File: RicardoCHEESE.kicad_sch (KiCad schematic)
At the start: 37 parts, among them J101 RBUS, U101 ESP32-S3, Y101 40MHz±10ppm

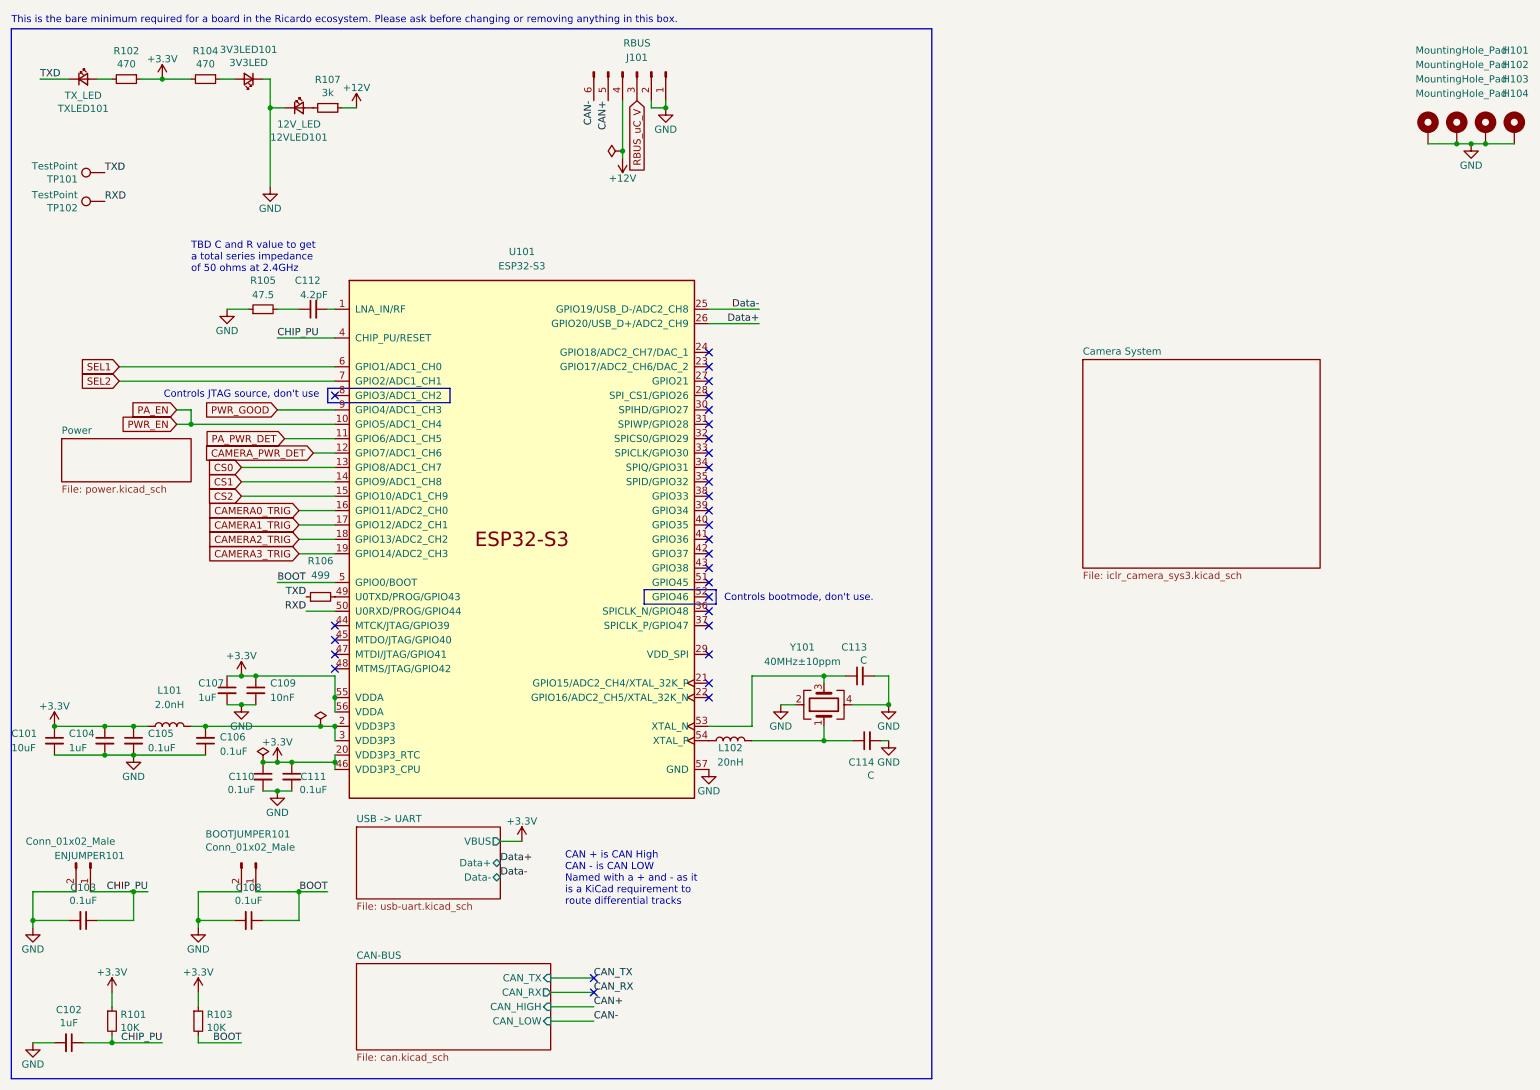
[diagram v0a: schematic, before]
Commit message: File names and ERC
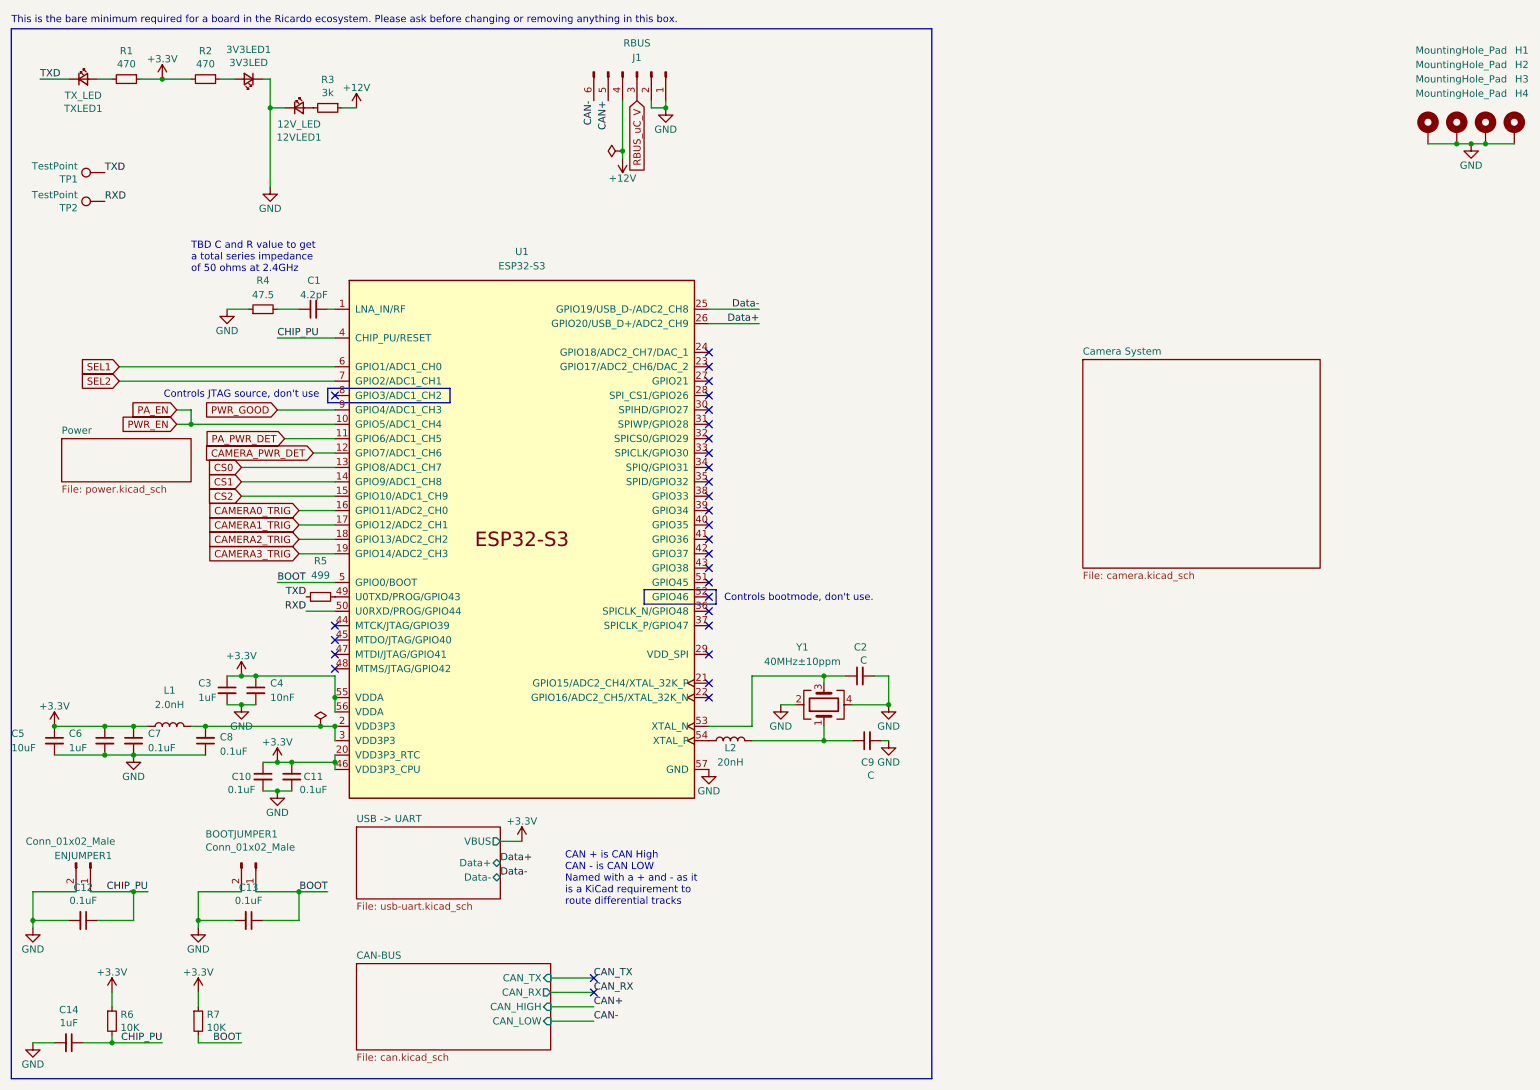
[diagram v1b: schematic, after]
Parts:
- renumbered 12VLED101 to 12VLED1, 3V3LED101 to 3V3LED1, BOOTJUMPER101 to BOOTJUMPER1, C112 to C1, C110 to C10, C111 to C11, C103 to C12, C108 to C13, C102 to C14, C113 to C2, C107 to C3, C109 to C4, C101 to C5, C104 to C6, C105 to C7, C106 to C8, C114 to C9, ENJUMPER101 to ENJUMPER1, H101 to H1, H102 to H2, H103 to H3, H104 to H4, J101 to J1, L101 to L1, L102 to L2, R102 to R1, R104 to R2, R107 to R3, R105 to R4, R106 to R5, R101 to R6, R103 to R7, TP101 to TP1, TP102 to TP2, TXLED101 to TXLED1, U101 to U1, Y101 to Y1
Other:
- sheet Camera System: file iclr_camera_sys3.kicad_sch -> camera.kicad_sch

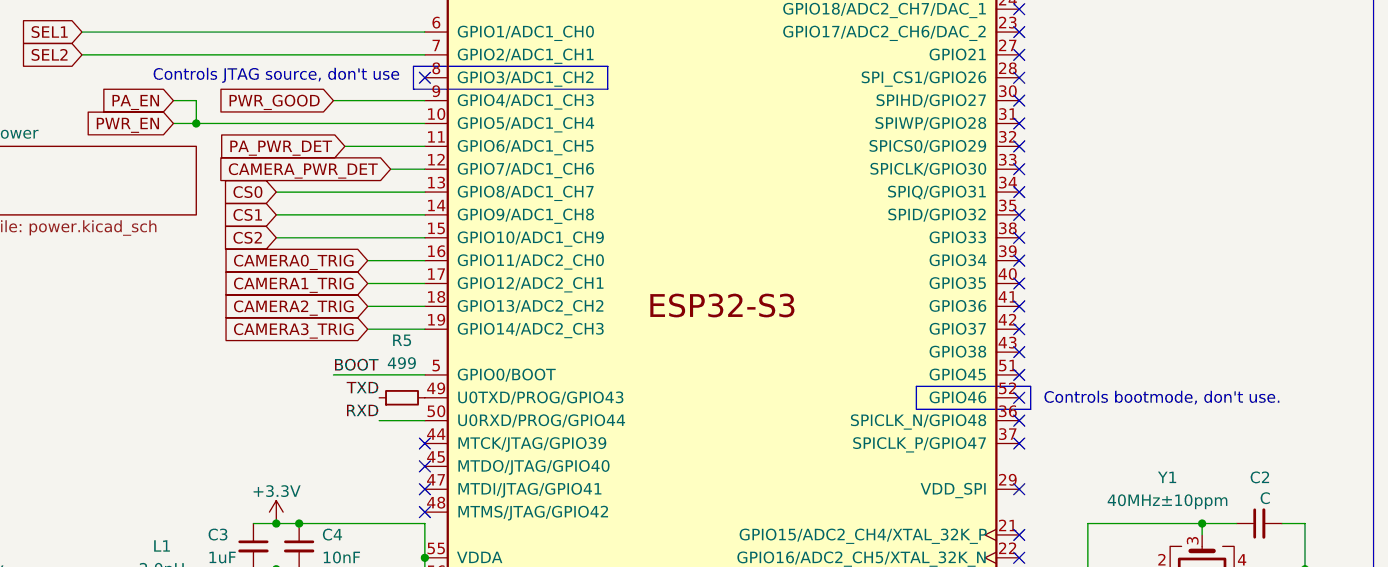
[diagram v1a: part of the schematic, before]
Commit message: Add photo triggers
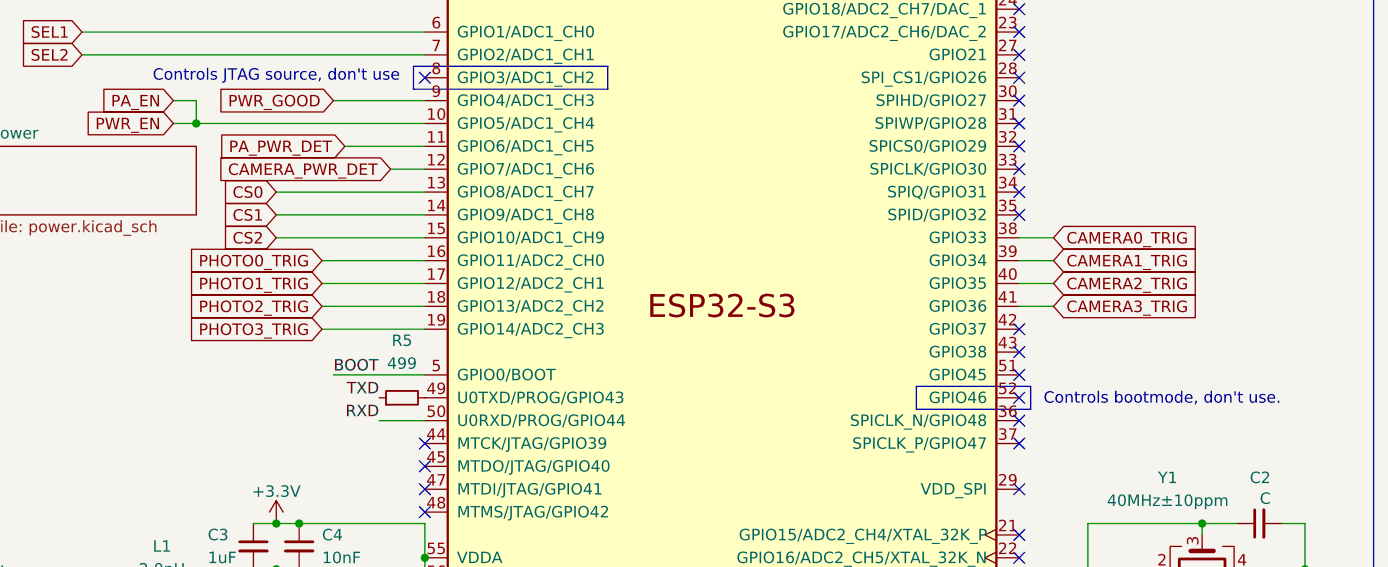
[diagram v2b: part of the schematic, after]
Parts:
- U1: footprint iclr:QFN40P700X700X90-57N -> fps:QFN40P700X700X90-57N
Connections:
- net CAMERA0_TRIG: now also U1.38 (GPIO33); no longer U1.16 (GPIO11/ADC2_CH0)
- net CAMERA1_TRIG: now also U1.39 (GPIO34); no longer U1.17 (GPIO12/ADC2_CH1)
- net CAMERA2_TRIG: now also U1.40 (GPIO35); no longer U1.18 (GPIO13/ADC2_CH2)
- net CAMERA3_TRIG: now also U1.41 (GPIO36); no longer U1.19 (GPIO14/ADC2_CH3)
- new net PHOTO0_TRIG: U1.16 (GPIO11/ADC2_CH0)
- new net PHOTO1_TRIG: U1.17 (GPIO12/ADC2_CH1)
- new net PHOTO2_TRIG: U1.18 (GPIO13/ADC2_CH2)
- new net PHOTO3_TRIG: U1.19 (GPIO14/ADC2_CH3)
- no-connect marks 30 -> 26
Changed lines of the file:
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@@
   (no_connect (at 135.89 69.85))
   (no_connect (at 135.89 107.95))
-  (no_connect (at 135.89 100.33))
   (no_connect (at 115.57 182.88))
   (no_connect (at 135.89 87.63))
-  (no_connect (at 135.89 102.87))
-  (no_connect (at 135.89 95.25))
   (no_connect (at 135.89 115.57))
   (no_connect (at 135.89 82.55))
@@
   (no_connect (at 69.85 77.47))
   (no_connect (at 135.89 118.11))
-  (no_connect (at 135.89 97.79))
   (no_connect (at 69.85 120.65))
   (no_connect (at 135.89 72.39))
@@
     (stroke (width 0) (type default))
   )
-  (wire (pts (xy 63.5 97.79) (xy 69.85 97.79))
-    (stroke (width 0) (type default))
-  )
   (wire (pts (xy 60.96 26.67) (xy 58.42 26.67))
     (stroke (width 0) (type default))
@@
     (stroke (width 0) (type default))
   )
+  (wire (pts (xy 58.42 105.41) (xy 69.85 105.41))
+    (stroke (width 0) (type default))
+  )
   (wire (pts (xy 128.27 25.4) (xy 128.27 26.67))
     (stroke (width 0) (type default))
@@
     (stroke (width 0) (type default))
   )
+  (wire (pts (xy 135.89 102.87) (xy 139.7 102.87))
+    (stroke (width 0) (type default))
+  )
   (wire (pts (xy 45.72 165.1) (xy 53.34 165.1))
     (stroke (width 0) (type default))
@@
     (stroke (width 0) (type default))
   )
+  (wire (pts (xy 135.89 97.79) (xy 139.7 97.79))
+    (stroke (width 0) (type default))
+  )
   (wire (pts (xy 267.97 33.02) (xy 262.89 33.02))
     (stroke (width 0) (type default))
@@
     (stroke (width 0) (type default))
   )
-  (wire (pts (xy 63.5 100.33) (xy 69.85 100.33))
-    (stroke (width 0) (type default))
-  )
   (wire (pts (xy 55.88 127) (xy 69.85 127))
     (stroke (width 0) (type default))
@@
     (stroke (width 0) (type default))
   )
+  (wire (pts (xy 58.42 102.87) (xy 69.85 102.87))
+    (stroke (width 0) (type default))
+  )
   (wire (pts (xy 148.59 132.08) (xy 151.13 132.08))
     (stroke (width 0) (type default))
@@
     (stroke (width 0) (type default))
   )
-  (wire (pts (xy 63.5 105.41) (xy 69.85 105.41))
-    (stroke (width 0) (type default))
-  )
   (wire (pts (xy 59.69 67.31) (xy 69.85 67.31))
     (stroke (width 0) (type default))
@@
     (stroke (width 0) (type default))
   )
-  (wire (pts (xy 63.5 102.87) (xy 69.85 102.87))
-    (stroke (width 0) (type default))
-  )
   (wire (pts (xy 20.32 135.89) (xy 29.21 135.89))
     (stroke (width 0) (type default))
@@
     (stroke (width 0) (type default))
   )
+  (wire (pts (xy 58.42 97.79) (xy 69.85 97.79))
+    (stroke (width 0) (type default))
+  )
   (wire (pts (xy 41.91 80.01) (xy 44.45 80.01))
     (stroke (width 0) (type default))
@@
     (stroke (width 0) (type default))
   )
+  (wire (pts (xy 58.42 100.33) (xy 69.85 100.33))
+    (stroke (width 0) (type default))
+  )
   (wire (pts (xy 31.75 72.39) (xy 69.85 72.39))
     (stroke (width 0) (type default))
@@
     (stroke (width 0) (type default))
   )
+  (wire (pts (xy 135.89 100.33) (xy 139.7 100.33))
+    (stroke (width 0) (type default))
+  )
   (wire (pts (xy 34.29 140.97) (xy 46.99 140.97))
     (stroke (width 0) (type default))
@@
   )
   (wire (pts (xy 57.15 142.24) (xy 59.69 142.24))
+    (stroke (width 0) (type default))
+  )
+  (wire (pts (xy 135.89 95.25) (xy 139.7 95.25))
     (stroke (width 0) (type default))
   )
@@
     )
   )
-  (global_label "CAMERA0_TRIG" (shape input) (at 63.5 97.79 180) (fields_autoplaced)
+  (global_label "CAMERA0_TRIG" (shape input) (at 139.7 95.25 0) (fields_autoplaced)
+    (effects (font (size 1.27 1.27)) (justify left))
+    (property "Intersheetrefs" "${INTERSHEET_REFS}" (at 155.6313 95.1706 0)
+      (effects (font (size 1.27 1.27)) (justify left) hide)
+    )
+  )
+  (global_label "PHOTO0_TRIG" (shape input) (at 58.42 97.79 180) (fields_autoplaced)
     (effects (font (size 1.27 1.27)) (justify right))
-    (property "Intersheetrefs" "${INTERSHEET_REFS}" (at 47.5687 97.7106 0)
+    (property "Intersheetrefs" "${INTERSHEET_REFS}" (at 43.6498 97.79 0)
       (effects (font (size 1.27 1.27)) (justify right) hide)
     )
   )
-  (global_label "CAMERA2_TRIG" (shape input) (at 63.5 102.87 180) (fields_autoplaced)
-    (effects (font (size 1.27 1.27)) (justify right))
-    (property "Intersheetrefs" "${INTERSHEET_REFS}" (at 47.5687 102.7906 0)
-      (effects (font (size 1.27 1.27)) (justify right) hide)
+  (global_label "CAMERA2_TRIG" (shape input) (at 139.7 100.33 0) (fields_autoplaced)
+    (effects (font (size 1.27 1.27)) (justify left))
+    (property "Intersheetrefs" "${INTERSHEET_REFS}" (at 155.6313 100.2506 0)
+      (effects (font (size 1.27 1.27)) (justify left) hide)
     )
   )
@@
     )
   )
+  (global_label "PHOTO2_TRIG" (shape input) (at 58.42 102.87 180) (fields_autoplaced)
+    (effects (font (size 1.27 1.27)) (justify right))
+    (property "Intersheetrefs" "${INTERSHEET_REFS}" (at 43.6498 102.87 0)
+      (effects (font (size 1.27 1.27)) (justify right) hide)
+    )
+  )
+  (global_label "PHOTO1_TRIG" (shape input) (at 58.42 100.33 180) (fields_autoplaced)
+    (effects (font (size 1.27 1.27)) (justify right))
+    (property "Intersheetrefs" "${INTERSHEET_REFS}" (at 43.6498 100.33 0)
+      (effects (font (size 1.27 1.27)) (justify right) hide)
+    )
+  )
   (global_label "PA_PWR_DET" (shape input) (at 60.96 85.09 180) (fields_autoplaced)
     (effects (font (size 1.27 1.27)) (justify right))
@@
     )
   )
+  (global_label "PHOTO3_TRIG" (shape input) (at 58.42 105.41 180) (fields_autoplaced)
+    (effects (font (size 1.27 1.27)) (justify right))
+    (property "Intersheetrefs" "${INTERSHEET_REFS}" (at 43.6498 105.41 0)
+      (effects (font (size 1.27 1.27)) (justify right) hide)
+    )
+  )
   (global_label "CAMERA_PWR_DET" (shape input) (at 66.04 87.63 180) (fields_autoplaced)
     (effects (font (size 1.27 1.27)) (justify right))
@@
     )
   )
-  (global_label "CAMERA1_TRIG" (shape input) (at 63.5 100.33 180) (fields_autoplaced)
-    (effects (font (size 1.27 1.27)) (justify right))
-    (property "Intersheetrefs" "${INTERSHEET_REFS}" (at 47.5687 100.2506 0)
-      (effects (font (size 1.27 1.27)) (justify right) hide)
+  (global_label "CAMERA1_TRIG" (shape input) (at 139.7 97.79 0) (fields_autoplaced)
+    (effects (font (size 1.27 1.27)) (justify left))
+    (property "Intersheetrefs" "${INTERSHEET_REFS}" (at 155.6313 97.7106 0)
+      (effects (font (size 1.27 1.27)) (justify left) hide)
     )
   )
@@
     )
   )
-  (global_label "CAMERA3_TRIG" (shape input) (at 63.5 105.41 180) (fields_autoplaced)
-    (effects (font (size 1.27 1.27)) (justify right))
-    (property "Intersheetrefs" "${INTERSHEET_REFS}" (at 47.5687 105.3306 0)
-      (effects (font (size 1.27 1.27)) (justify right) hide)
+  (global_label "CAMERA3_TRIG" (shape input) (at 139.7 102.87 0) (fields_autoplaced)
+    (effects (font (size 1.27 1.27)) (justify left))
+    (property "Intersheetrefs" "${INTERSHEET_REFS}" (at 155.6313 102.7906 0)
+      (effects (font (size 1.27 1.27)) (justify left) hide)
     )
   )
@@
       (effects (font (size 1.27 1.27)))
     )
-    (property "Footprint" "iclr:QFN40P700X700X90-57N" (at 102.87 153.67 0)
-      (effects (font (size 1.27 1.27)) hide)
-    )
+    (property "Footprint" "fps:QFN40P700X700X90-57N" (at 102.87 153.67 0)
+      (effects (font (size 1.27 1.27)) hide)
+    )

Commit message: Some routing
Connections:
- net BOOT: now also C13.2; no longer C13.1
- net CHIP_PU: now also C14.2; no longer C14.1
- net GND: now also C13.1, C14.1; no longer C13.2, C14.2
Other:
- moved on the sheet: C13, C14
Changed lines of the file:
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@@
     )
   )
-  (symbol (lib_id "Device:C_Small") (at 22.86 191.77 270) (unit 1)
+  (symbol (lib_id "Device:C_Small") (at 22.86 191.77 90) (mirror x) (unit 1)
     (in_bom yes) (on_board yes) (dnp no)
     (property "Reference" "C14" (at 22.86 185.9534 90)
@@
     )
   )
-  (symbol (lib_id "Device:C_Small") (at 54.61 170.18 270) (unit 1)
+  (symbol (lib_id "Device:C_Small") (at 54.61 170.18 90) (mirror x) (unit 1)
     (in_bom yes) (on_board yes) (dnp no)
     (property "Reference" "C13" (at 54.61 164.3634 90)
